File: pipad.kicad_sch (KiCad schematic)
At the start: 1 part

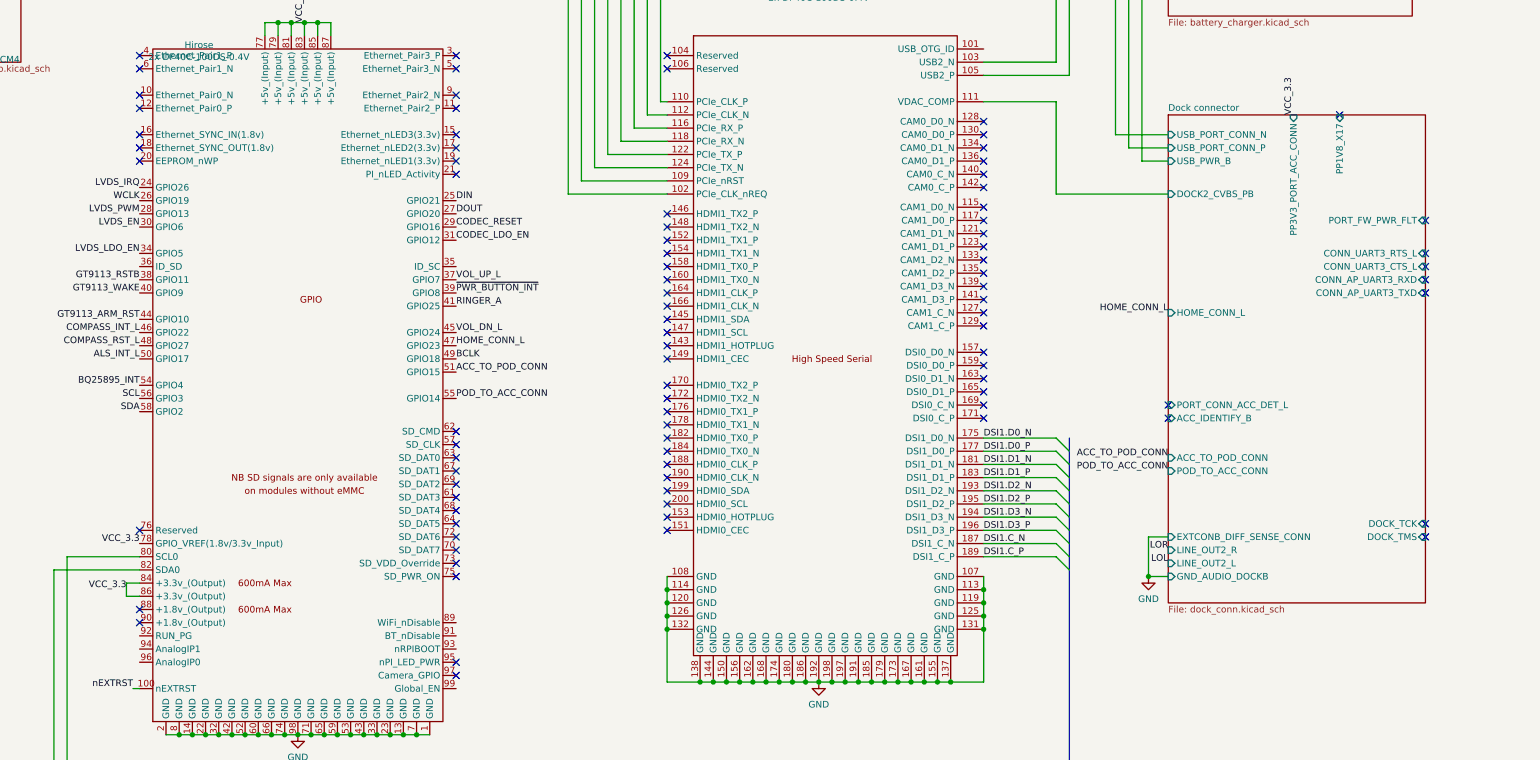
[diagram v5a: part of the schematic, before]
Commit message: Lots of tiny test points; add 3d models to a bunch of things. Re-length-match PCIe and DSI traces.
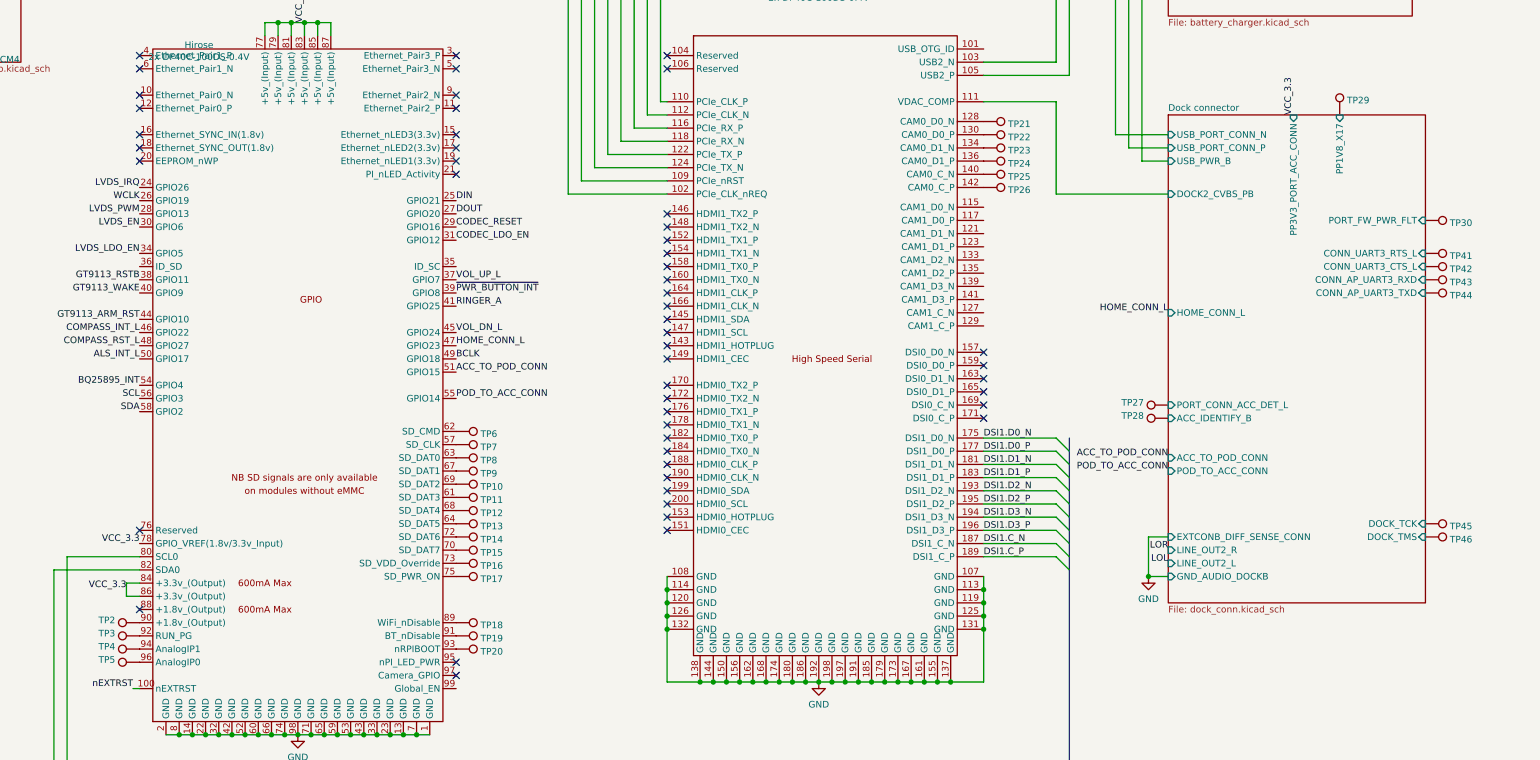
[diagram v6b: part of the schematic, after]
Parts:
- added TP10, TP11, TP12, TP13, TP14, TP15, TP16, TP17, TP18, TP19, TP2, TP20, TP21, TP22, TP23, TP24, TP25, TP26, TP27, TP28, TP29, TP3, TP30, TP4, TP41, TP42, TP43, TP44, TP45, TP46, TP5, TP6, TP7, TP8, TP9: TestPoint, footprints:testpoint_small, symbol Connector:TestPoint
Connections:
- net Dock connector/ACC_IDENTIFY_B: now also TP28.1
- net Dock connector/CONN_AP_UART3_RXD: now also TP43.1
- net Dock connector/CONN_AP_UART3_TXD: now also TP44.1
- net Dock connector/CONN_UART3_CTS_L: now also TP42.1
- net Dock connector/CONN_UART3_RTS_L: now also TP41.1
- net Dock connector/DOCK_TCK: now also TP45.1
- net Dock connector/DOCK_TMS: now also TP46.1
- net Dock connector/PORT_CONN_ACC_DET_L: now also TP27.1
- net Dock connector/PORT_FW_PWR_FLT: now also TP30.1
- net Dock connector/PP1V8_X17: now also TP29.1
- net at Module1.128 (CAM0_D0_N): now also TP21.1
- net at Module1.130 (CAM0_D0_P): now also TP22.1
- net at Module1.134 (CAM0_D1_N): now also TP23.1
- net at Module1.136 (CAM0_D1_P): now also TP24.1
- net at Module1.140 (CAM0_C_N): now also TP25.1
- net at Module1.142 (CAM0_C_P): now also TP26.1
- net at Module1.57 (SD_CLK): now also TP7.1
- net at Module1.61 (SD_DAT3): now also TP11.1
- net at Module1.62 (SD_CMD): now also TP6.1
- net at Module1.63 (SD_DAT0): now also TP8.1
- net at Module1.64 (SD_DAT5): now also TP13.1
- net at Module1.67 (SD_DAT1): now also TP9.1
- net at Module1.68 (SD_DAT4): now also TP12.1
- net at Module1.69 (SD_DAT2): now also TP10.1
- net at Module1.70 (SD_DAT7): now also TP15.1
- net at Module1.72 (SD_DAT6): now also TP14.1
- net at Module1.73 (SD_VDD_Override): now also TP16.1
- net at Module1.75 (SD_PWR_ON): now also TP17.1
- net at Module1.89 (WiFi_nDisable): now also TP18.1
- net at Module1.90 (+1.8v_(Output)): now also TP2.1
- net at Module1.91 (BT_nDisable): now also TP19.1
- net at Module1.92 (RUN_PG): now also TP3.1
- net at Module1.93 (nRPIBOOT): now also TP20.1
- net at Module1.94 (AnalogIP1): now also TP4.1
- net at Module1.96 (AnalogIP0): now also TP5.1
- no-connect marks 95 -> 56

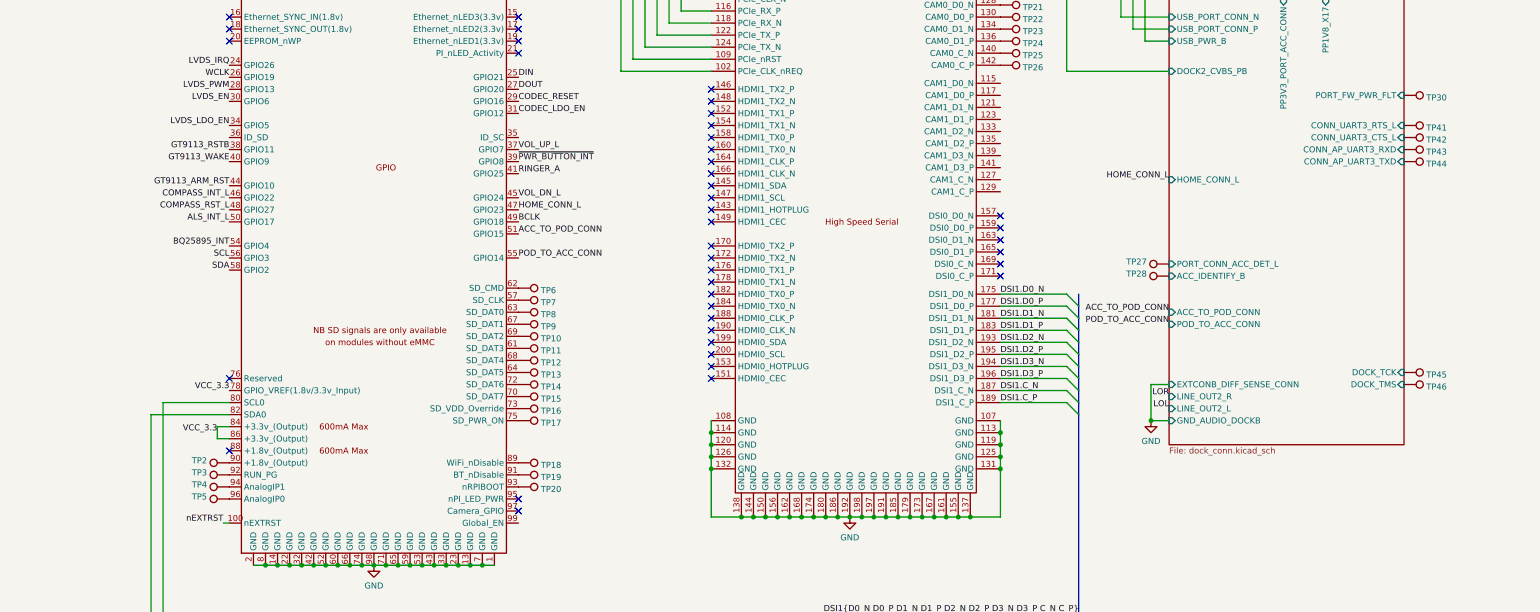
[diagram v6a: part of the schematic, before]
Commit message: Add a bunch more 3d models
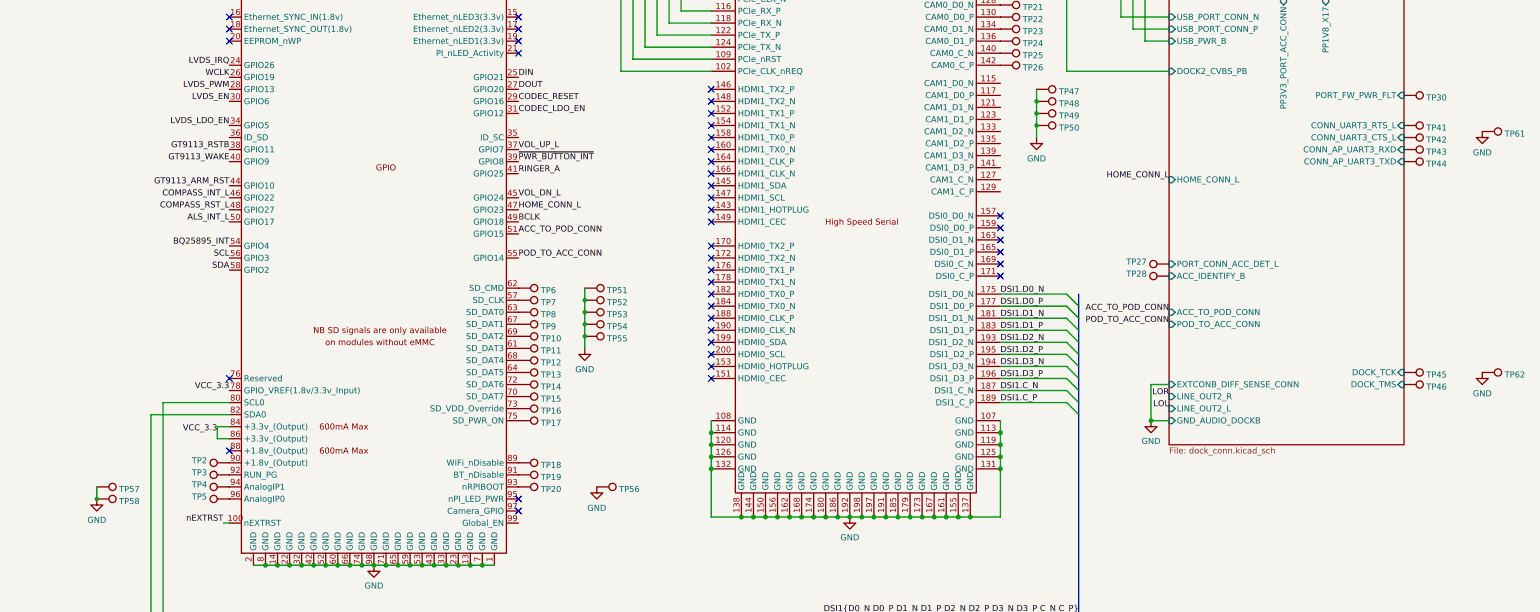
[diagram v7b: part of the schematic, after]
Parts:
- added TP47, TP48, TP49, TP50, TP51, TP52, TP53, TP54, TP55, TP56, TP57, TP58, TP61, TP62: TestPoint, footprints:testpoint_small, symbol Connector:TestPoint
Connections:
- net GND: now also TP47.1, TP48.1, TP49.1, TP50.1, TP51.1, TP52.1, TP53.1, TP54.1, TP55.1, TP56.1, TP57.1, TP58.1, TP61.1, TP62.1

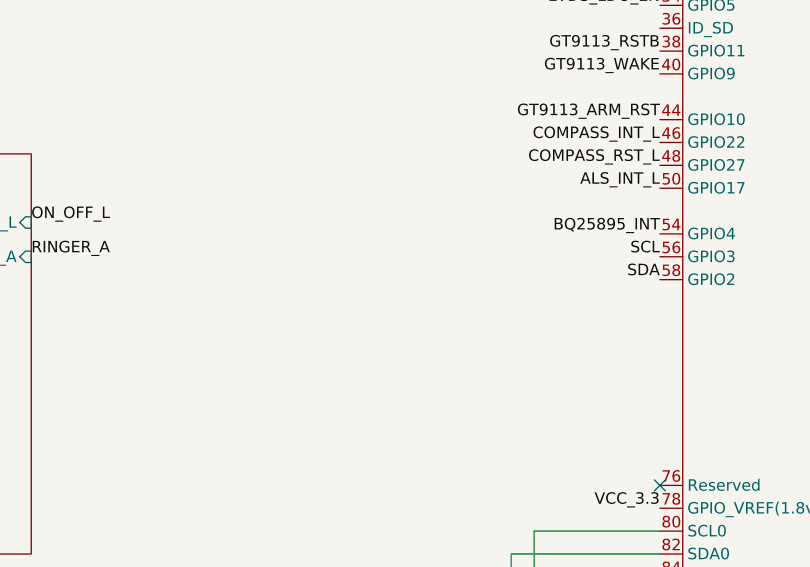
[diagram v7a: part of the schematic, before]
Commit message: Even more testpoints!
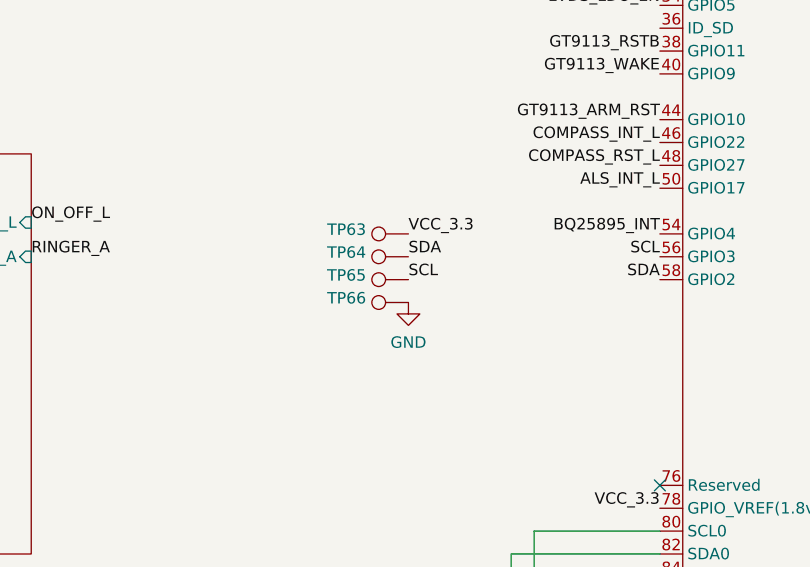
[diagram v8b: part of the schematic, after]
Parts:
- added TP63, TP64, TP65, TP66: TestPoint, footprints:testpoint_small, symbol Connector:TestPoint
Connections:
- net GND: now also TP66.1
- net SCL: now also TP65.1
- net SDA: now also TP64.1
- net VCC_3.3: now also TP63.1
